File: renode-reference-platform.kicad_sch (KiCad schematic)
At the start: 28 parts

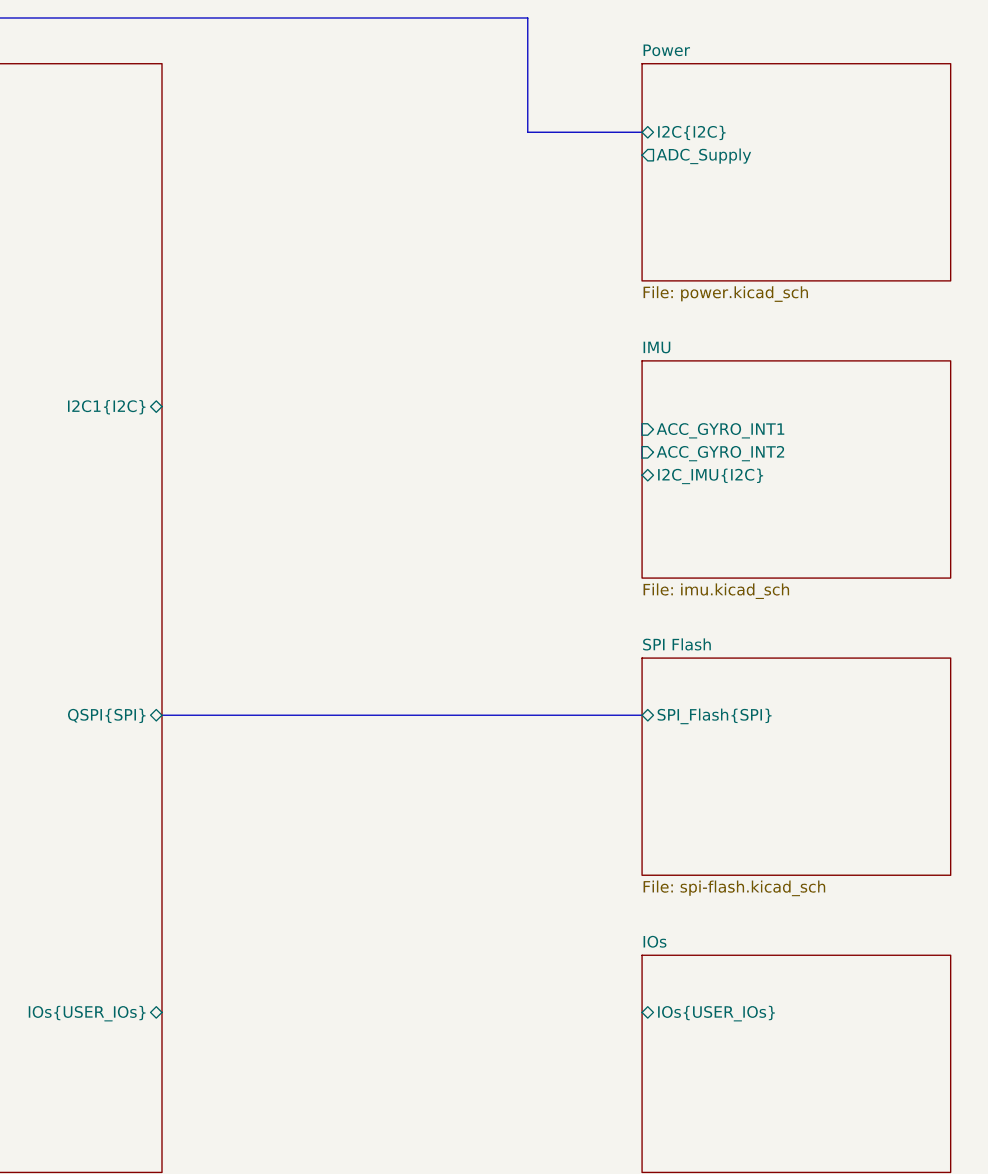
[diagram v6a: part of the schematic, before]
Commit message: [#95036] Reconnect IMU interupts
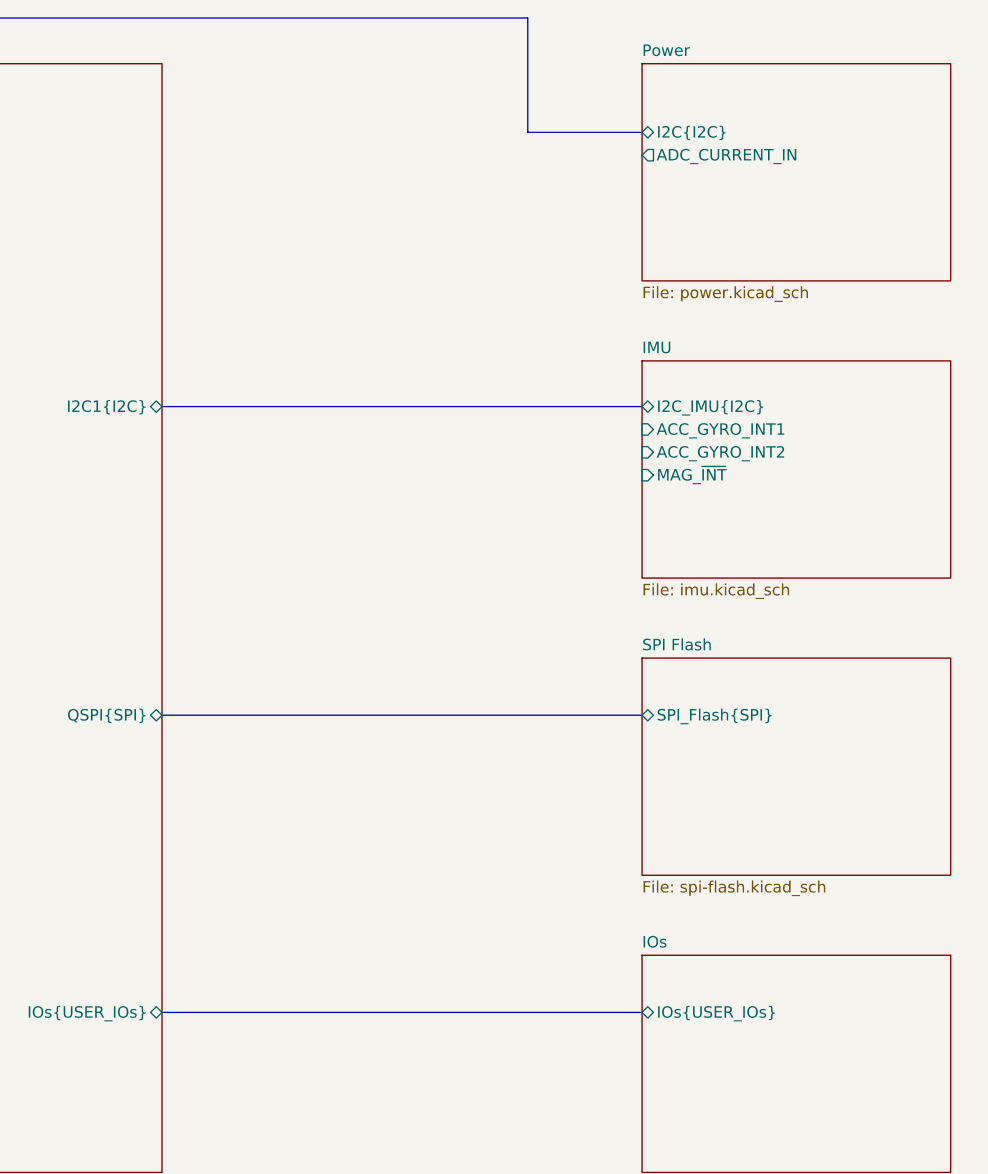
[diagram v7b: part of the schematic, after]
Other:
- sheet IMU ports: added MAG_~{INT}; removed none
- sheet Power ports: added ADC_CURRENT_IN; removed ADC_Supply
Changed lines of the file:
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@@
 	(bus
 		(pts
+			(xy 198.12 190.5) (xy 251.46 190.5)
+		)
+		(stroke
+			(width 0)
+			(type default)
+		)
+	)
+	(bus
+		(pts
 			(xy 119.38 91.44) (xy 119.38 80.01)
 		)
@@
 	(bus
 		(pts
+			(xy 198.12 123.19) (xy 251.46 123.19)
+		)
+		(stroke
+			(width 0)
+			(type default)
+		)
+	)
+	(bus
+		(pts
 			(xy 99.06 91.44) (xy 119.38 91.44)
 		)
@@
 		)
 		(pin "I2C_IMU{I2C}" bidirectional
+			(at 251.46 123.19 180)
+			(effects
+				(font
+					(size 1.27 1.27)
+				)
+				(justify left)
+			)
+		)
+		(pin "MAG_~{INT}" input
 			(at 251.46 130.81 180)
 			(effects
@@
 			)
 		)
-		(pin "ADC_Supply" output
-			(at 251.46 95.25 180)
+		(pin "I2C{I2C}" bidirectional
+			(at 251.46 92.71 180)
 			(effects
 				(font
@@
 			)
 		)
-		(pin "I2C{I2C}" bidirectional
-			(at 251.46 92.71 180)
+		(pin "ADC_CURRENT_IN" output
+			(at 251.46 95.25 180)
 			(effects
 				(font

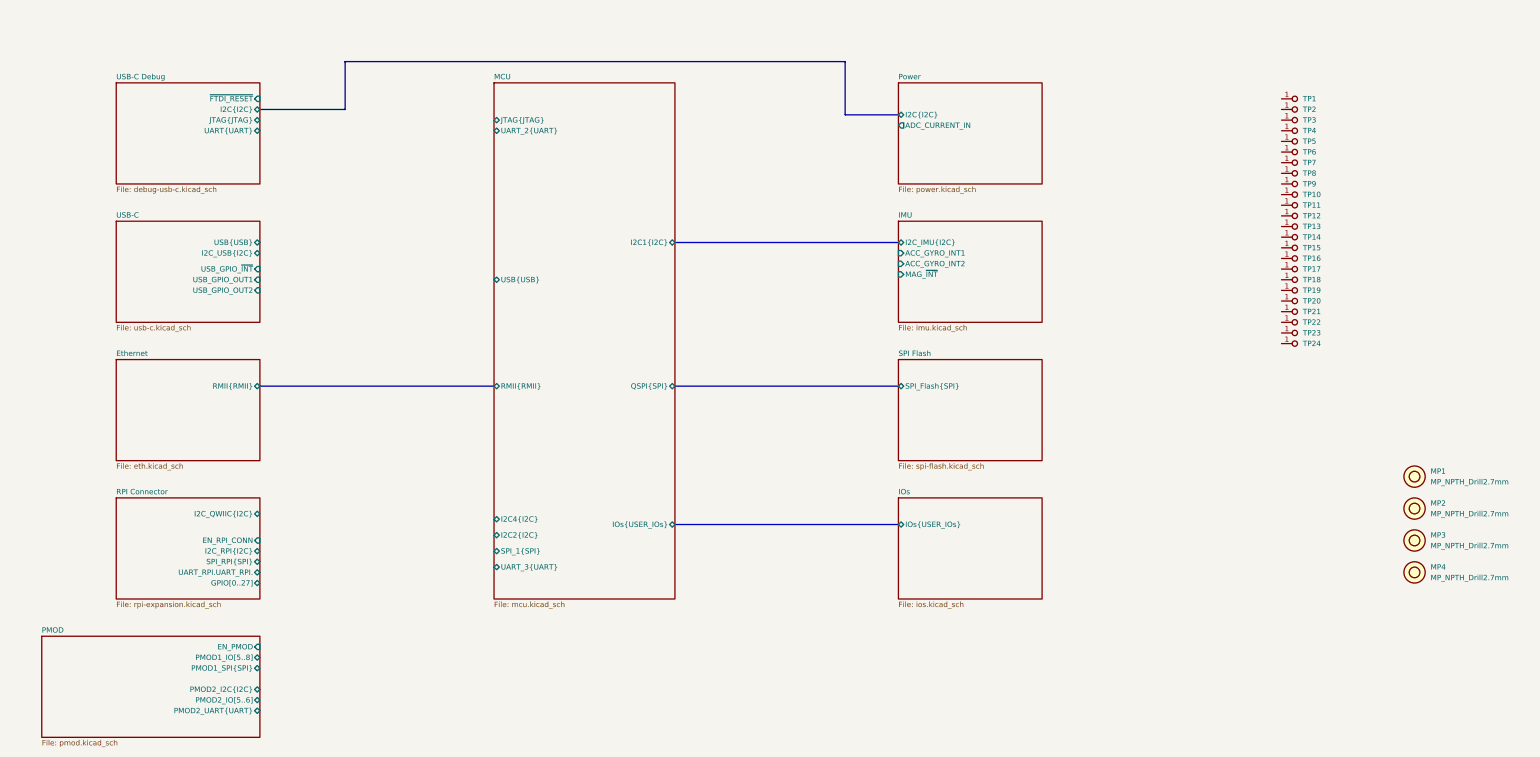
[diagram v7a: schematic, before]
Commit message: [#95036] Manage I2C, UART, SPI interfaces for RPI and PMOD connectors
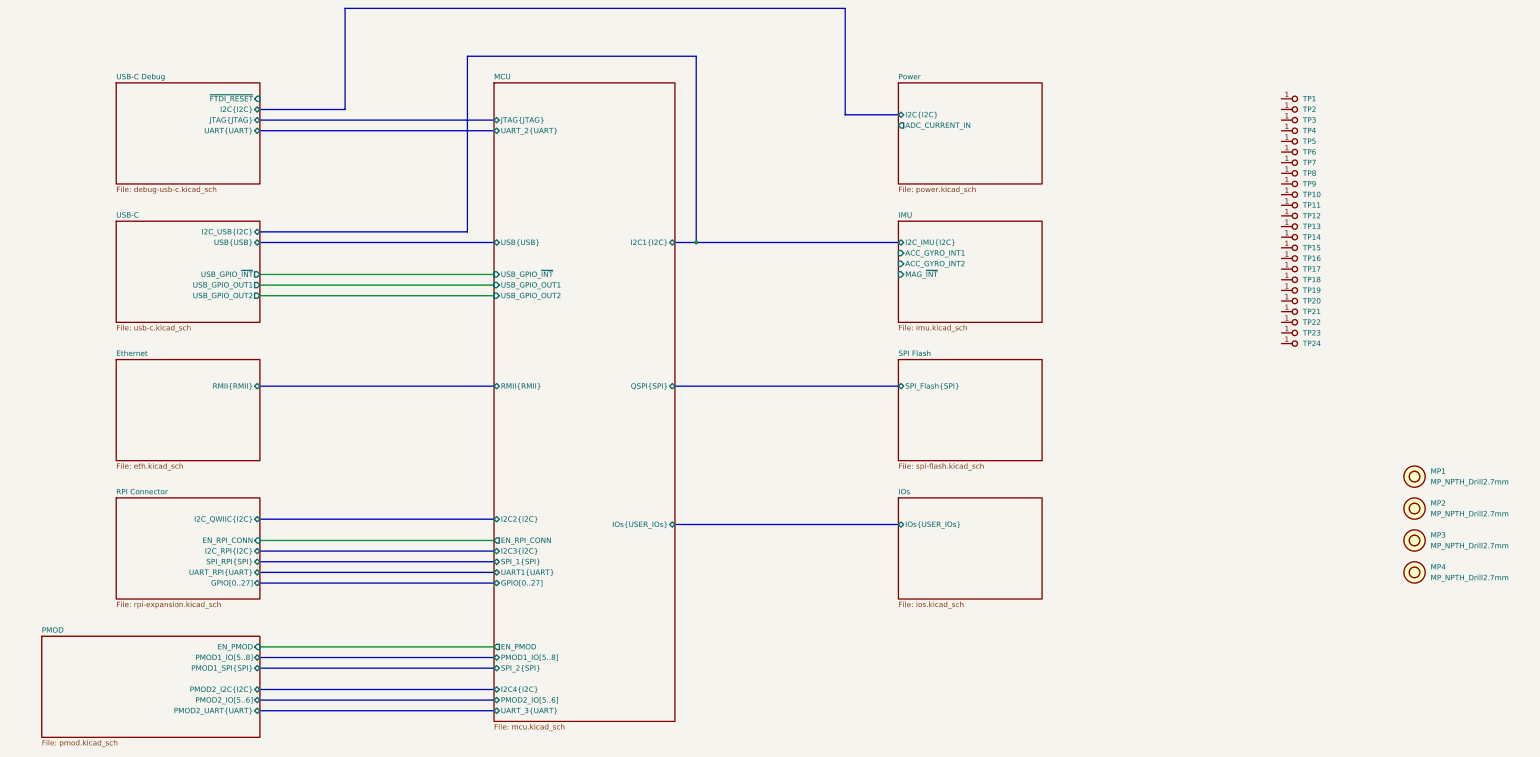
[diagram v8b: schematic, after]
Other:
- sheet MCU ports: added EN_PMOD, EN_RPI_CONN, GPIO[0..27], I2C3{I2C}, PMOD1_IO[5..8], PMOD2_IO[5..6], SPI_2{SPI}, UART1{UART}, USB_GPIO_OUT1, USB_GPIO_OUT2, USB_GPIO_~{INT}; removed none
- sheet RPI Connector ports: added UART_RPI{UART}; removed UART_RPI.UART_RPI.
